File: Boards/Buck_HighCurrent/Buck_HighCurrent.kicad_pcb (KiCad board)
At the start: 2 copper layers, 25 parts, among them U1 TPS563231

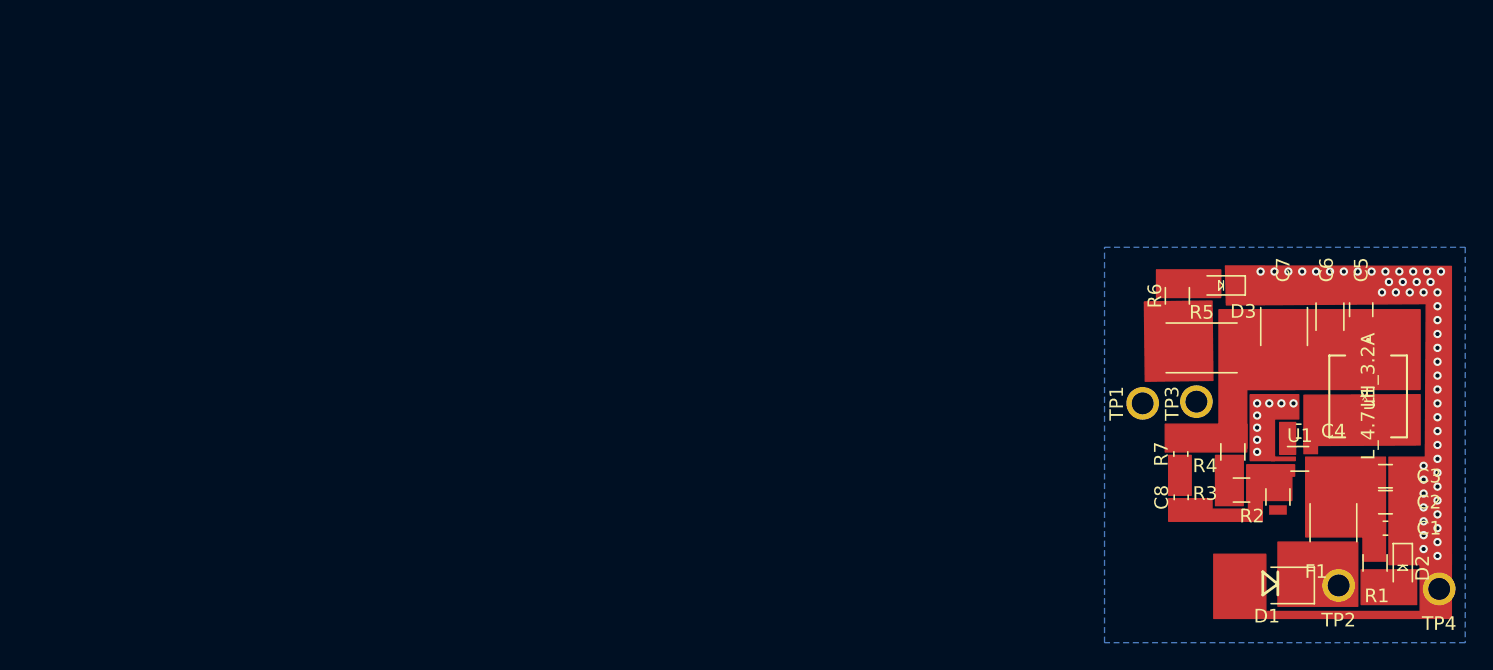
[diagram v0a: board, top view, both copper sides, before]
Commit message: first pass layout with new buck.
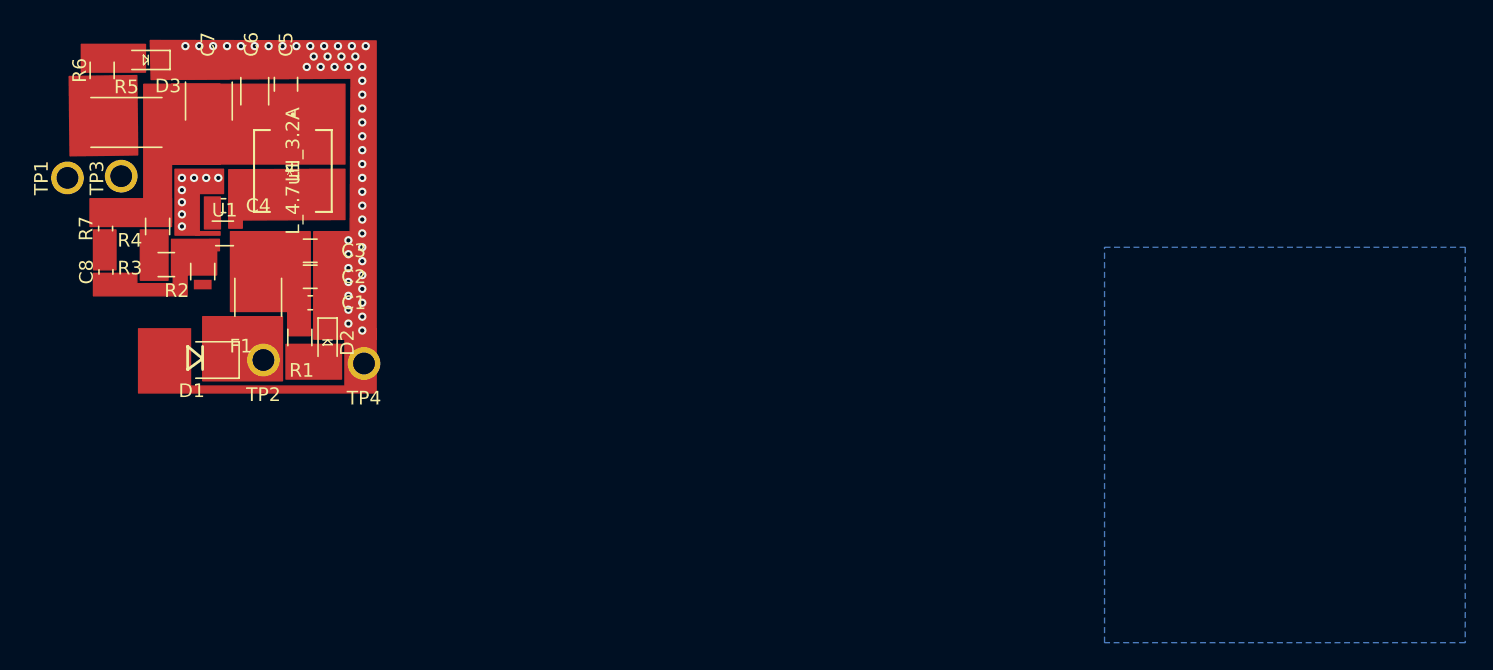
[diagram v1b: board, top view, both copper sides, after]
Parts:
- moved C1 80.5 mm to (-11.4, 27.9)
- moved C2 80.5 mm to (-11.4, 26.0)
- moved C3 80.5 mm to (-11.4, 24.1)
- moved C4 80.5 mm to (-17.8, 20.8)
- moved C6 80.5 mm to (-15.5, 12.4)
- moved L1 80.5 mm to (-12.7, 18.3)
- moved R1 80.5 mm to (-12.2, 30.5)
- moved R4 80.5 mm to (-22.6, 22.4)
- moved R6 80.5 mm to (-26.7, 10.9)
- moved TP1 80.5 mm to (-29.2, 18.8)
- moved U1 80.5 mm to (-17.7, 22.9)
- moved C5 80.5 mm to (-13.2, 11.9)
- moved C7 80.5 mm to (-18.9, 13.2)
- moved C8 80.5 mm to (-26.4, 25.7)
- moved D1 80.5 mm to (-19.8, 32.1)
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
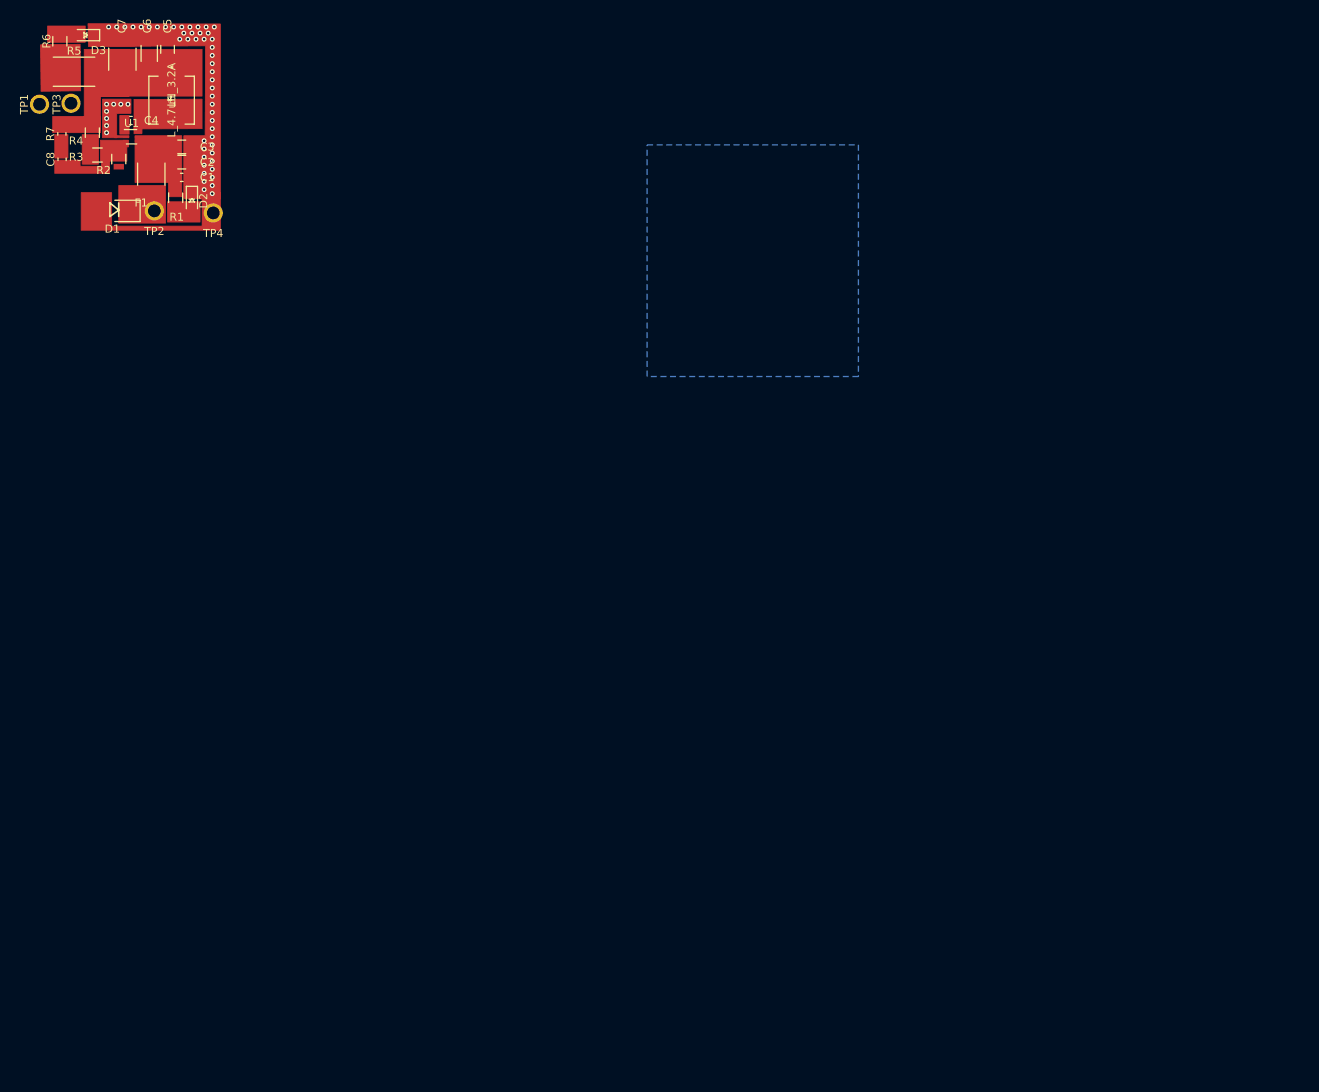
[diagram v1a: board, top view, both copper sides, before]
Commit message: 3A buck, rev2.0, no magic smoke now
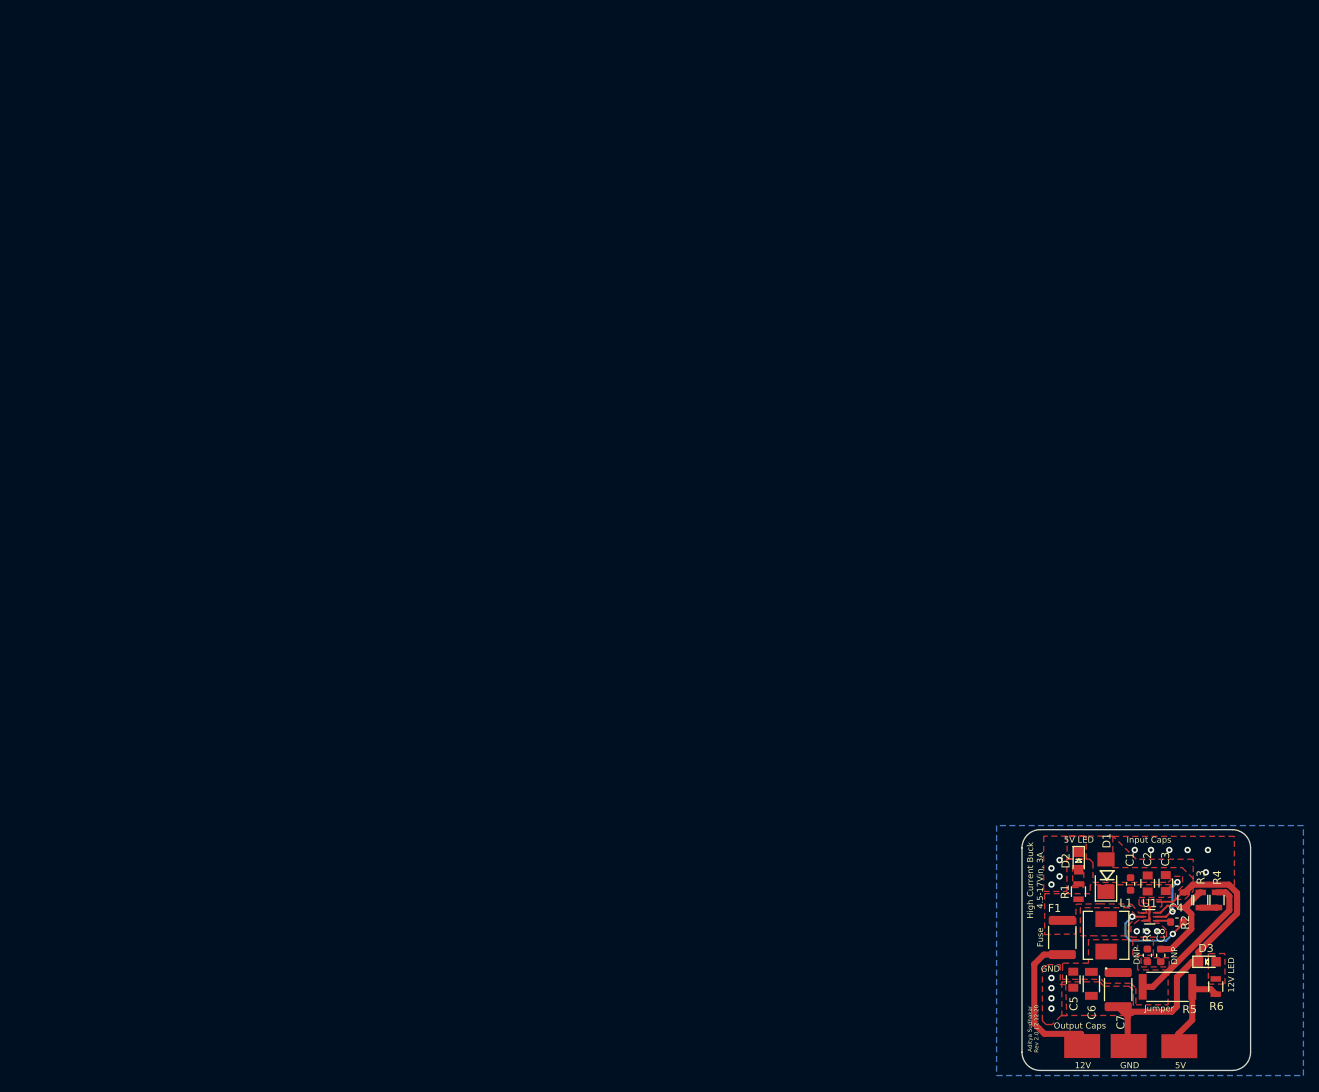
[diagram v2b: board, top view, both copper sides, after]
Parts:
- removed TP4: TP, footprints:tp_1.6mm
- C8: value C_100nF -> C_100nF_DNP
- R1: value R_200 -> R_1K
- R7: value R_1 -> R_1_DNP
- TP1, TP2, TP3: value TP -> Test_Point_SMD; footprint footprints:tp_1.6mm -> footprints:Test_Point_SMD
- U1: footprint footprints:SOT-563 -> Package_TO_SOT_SMD:SOT-563
- moved R6 186.7 mm to (117.8, 129.1)
- moved D3 181.9 mm to (116.8, 126.0), turned to 0 degrees
- moved R5 178.2 mm to (111.8, 129.1), turned to 180 degrees
- moved TP3 177.1 mm to (106.9, 136.5)
- moved TP1 175.6 mm to (101.1, 136.5)
- moved C7 170.4 mm to (105.6, 129.5), turned to 270 degrees
- moved R4 170.2 mm to (118.0, 118.3)
- moved R7 170.2 mm to (109.3, 125.2)
- moved C8 169.6 mm to (110.9, 125.2), turned to 270 degrees
- moved R3 166.4 mm to (115.9, 118.3), turned to 90 degrees
- moved C6 165.5 mm to (102.3, 128.8), turned to 270 degrees
- moved TP2 165.3 mm to (113.3, 136.5)
- moved C4 164.7 mm to (113.0, 121.0)
- moved C5 162.3 mm to (100.0, 128.2), turned to 270 degrees
- moved R2 162.3 mm to (114.0, 118.3), turned to 90 degrees
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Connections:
- D1 pad 1: /12V -> Net-(C1-Pad1)
- TP1 pad 1: GND -> /12V
- TP2 pad 1: /12V -> VCC
- TP3 pad 1: VCC -> GND
- U1 pad 1: Net-(C4-Pad2) -> Net-(C1-Pad1)
- U1 pad 2: GND -> Net-(C4-Pad1)
- U1 pad 3: Net-(C8-Pad1) -> GND
- U1 pad 4: Net-(C1-Pad1) -> Net-(C4-Pad2)
- U1 pad 6: Net-(C4-Pad1) -> Net-(C8-Pad1)
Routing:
- net GND: track 1.48 -> 44.9 mm, vias 57 -> 17
- net /12V: track 0.00 -> 19.4 mm
- net Net-(C5-Pad1): track 0.00 -> 18.3 mm
- net Net-(C8-Pad1): track 1.07 -> 14.8 mm
- net Net-(C4-Pad1): track 0.05 -> 12.7 mm, vias 0 -> 2
- net VCC: track 0.00 -> 11.5 mm
- net Net-(C1-Pad1): track 0.75 -> 8.21 mm, vias 0 -> 2
- net Net-(R3-Pad1): track 0.00 -> 2.04 mm
- net Net-(C4-Pad2): track 0.05 -> 1.94 mm
- added copper zone on F.Cu, net GND
- added copper zone on F.Cu, net Net-(C1-Pad1)
- added copper zone on F.Cu, net Net-(C4-Pad1)
- added copper zone on F.Cu, net Net-(C5-Pad1)
- added copper zone on F.Cu, net Net-(C8-Pad2)
- added copper zone on F.Cu, net Net-(D2-Pad2)
- added copper zone on F.Cu, net Net-(D3-Pad2)
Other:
- board outline added: 28.6 x 30.1 mm
- board text added: "12V"
- board text added: "12V LED"
- board text added: "5V"
- board text added: "5V LED"
- board text added: "Aditya Sudhakar Rev 2.0 | 2.12.20"
- board text added: "DNP"
- board text added: "Fuse"
- board text added: "GND"
- board text added: "High Current Buck 4.5-17Vin, 3A"
- board text added: "Input Caps"
- board text added: "Jumper"
- board text added: "Output Caps"
